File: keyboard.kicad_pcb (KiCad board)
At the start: 2 copper layers, 121 parts, among them P2 CONN_02X03, SW1 SW_PUSH, SW10 SW_PUSH, SW11 SW_PUSH, SW12 SW_PUSH, SW13 SW_PUSH, SW14 SW_PUSH, SW15 SW_PUSH, SW16 SW_PUSH, SW17 SW_PUSH, SW18 SW_PUSH, SW19 SW_PUSH, SW2 SW_PUSH, SW20 SW_PUSH, SW21 SW_PUSH, SW22 SW_PUSH, SW23 SW_PUSH, SW24 SW_PUSH, SW25 SW_PUSH, SW26 SW_PUSH, SW27 SW_PUSH, SW28 SW_PUSH, SW29 SW_PUSH, SW3 SW_PUSH, SW30 SW_PUSH, SW31 SW_PUSH, SW32 SW_PUSH, SW33 SW_PUSH, SW34 SW_PUSH, SW35 SW_PUSH, SW36 SW_PUSH, SW37 SW_PUSH, SW38 SW_PUSH, SW39 SW_PUSH, SW4 SW_PUSH, SW40 SW_PUSH, SW41 SW_PUSH, SW42 SW_PUSH, SW43 SW_PUSH, SW44 SW_PUSH, SW45 SW_PUSH, SW5 SW_PUSH, SW6 SW_PUSH, SW7 SW_PUSH, SW8 SW_PUSH, SW9 SW_PUSH, U1 ATmega32U4, X1 CRYSTAL_SMD

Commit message: right hand side initial layout
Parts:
- moved SW2 459.2 mm to (279.2, 71.5)
- moved SW4 457.2 mm to (301.9, 78.5)
- moved SW3 422.5 mm to (281.9, 84.5)
- moved SW10 411.4 mm to (237.0, 80.1)
- moved SW5 402.4 mm to (258.3, 43.3)
- moved SW9 398.5 mm to (236.2, 57.5)
- moved SW6 383.2 mm to (258.2, 62.6)
- moved SW13 379.9 mm to (217.4, 91.0)
- moved SW8 369.9 mm to (235.3, 41.0)
- moved SW15 363.8 mm to (195.7, 68.0)
- moved SW11 362.7 mm to (213.9, 50.3)
- moved SW12 362.4 mm to (214.5, 66.3)
- moved SW7 359.2 mm to (257.6, 83.1)
- moved SW14 357.2 mm to (194.3, 52.5)
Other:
- board text added: "right side"

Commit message: picoflex connectors & good idea of board layout
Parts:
- added P10: CONN_01X01, Mounting_Holes:MountingHole_3mm, F.Cu at (272.0, 115.3)
- added P3: CONN_01X01, Mounting_Holes:MountingHole_3mm, F.Cu at (92.9, 52.0)
- added P4: CONN_01X01, Mounting_Holes:MountingHole_3mm, F.Cu at (23.4, 111.4)
- added P5: CONN_01X01, Mounting_Holes:MountingHole_3mm, F.Cu at (252.5, 62.0)
- added P6: CONN_01X01, Mounting_Holes:MountingHole_3mm, F.Cu at (163.6, 100.6)
- added P7: CONN_01X01, Mounting_Holes:MountingHole_3mm, F.Cu at (201.9, 56.6)
- added P8: CONN_01X01, Mounting_Holes:MountingHole_3mm, F.Cu at (112.2, 100.8)
- added P9: CONN_01X01, Mounting_Holes:MountingHole_3mm, F.Cu at (42.4, 58.0)
- conn1, conn2: footprint Pin_Headers:Pin_Header_Straight_2x08 -> fp:PICOFLEX-90814-16
- moved D5 418.6 mm to (243.2, 75.3)
- moved D6 398.6 mm to (234.9, 94.4)
- moved D3 380.5 mm to (257.6, 100.1)
- moved D8 378.8 mm to (220.8, 70.8)
- moved D7 375.7 mm to (212.3, 70.7)
- moved led1 375.0 mm to (267.5, 101.1), turned to 86.2 degrees
- moved D2 361.8 mm to (248.2, 114.0), turned to 90 degrees
- moved D9 360.5 mm to (215.3, 89.9)
- moved D13 349.1 mm to (178.6, 82.5), turned to 180 degrees
- moved led4 347.1 mm to (227.8, 72.1), turned to 180 degrees
- moved D10 346.9 mm to (199.7, 80.8)
- moved D4 343.9 mm to (233.6, 75.2)
- moved X1 338.9 mm to (265.2, 76.5), turned to 90 degrees
- moved D14 338.3 mm to (171.2, 82.9)
- moved led2 336.5 mm to (249.2, 94.5), turned to 180 degrees
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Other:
- board text added: "left side"

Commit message: libs and thumboard components done
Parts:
- removed SW16, SW17, SW18, SW19, SW20, SW21, SW22, SW23, SW38, SW39, SW40, SW41, SW42, SW43, SW44, SW45: SW_PUSH, fp:CHERRY_MX
- added S1: alps_4way, fp:alps 4way, F.Cu at (163.1, 181.1)
- added S2: alps_4way, fp:alps 4way, F.Cu at (162.6, 165.9)
- added S3: alps_4way, fp:alps 4way, F.Cu at (130.8, 145.0)
- added S4: alps_4way, fp:alps 4way, F.Cu at (130.8, 129.3)
- added U2: psp1000, fp:-JOYSTICK-PSP1000, F.Cu at (162.8, 165.9)
- added U3: psp1000, fp:-JOYSTICK-PSP1000, F.Cu at (130.6, 129.0)
- SW1: footprint fp:CHERRY_MX -> matt:SW_SPST_FSMSM
- moved SW1 400.7 mm to (278.6, 116.8), turned to 90 degrees
- moved led10 94.8 mm to (27.4, 96.8), turned to 273.8 degrees
- moved led13 76.4 mm to (108.2, 97.3), turned to 180 degrees
- moved D43 66.2 mm to (139.4, 139.2), turned to 90 degrees
- moved led15 65.8 mm to (108.7, 77.2), turned to 45 degrees
- moved led11 59.2 mm to (88.1, 95.0), turned to 180 degrees
- moved D41 58.9 mm to (120.1, 138.4), turned to 90 degrees
- moved led12 57.7 mm to (46.2, 90.9), turned to 180 degrees
- moved D44 55.7 mm to (139.4, 149.4), turned to 90 degrees
- moved D37 55.5 mm to (122.7, 144.0), turned to 270 degrees
- moved D40 55.2 mm to (139.4, 144.3), turned to 270 degrees
- moved led14 54.3 mm to (66.8, 90.2), turned to 180 degrees
- moved D42 51.7 mm to (120.1, 143.8), turned to 90 degrees
- moved D38 45.6 mm to (119.9, 149.6), turned to 270 degrees
- moved thumb-l2 45.1 mm to (125.7, 135.4)
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
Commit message: smt 4 ways
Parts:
- S1, S2, S3, S4: footprint fp:alps 4way -> fp:alps 4way smt
- moved SW26 198.5 mm to (207.6, 42.6), turned to 183.8 degrees
- moved P4 195.9 mm to (201.2, 29.2), turned to 180 degrees
- moved D25 183.9 mm to (202.4, 51.9), turned to 180 degrees
- moved led10 177.8 mm to (197.2, 43.9), turned to 93.8 degrees
- moved SW25 167.2 mm to (188.0, 34.9), turned to 183.8 degrees
- moved D23 164.8 mm to (190.4, 43.9), turned to 180 degrees
- moved SW24 157.4 mm to (189.3, 53.8), turned to 183.8 degrees
- moved D24 147.3 mm to (181.2, 44.4), turned to 180 degrees
- moved P9 142.1 mm to (182.3, 82.7), turned to 180 degrees
- moved led12 138.5 mm to (178.4, 49.7), turned to 0 degrees
- moved SW29 124.9 mm to (167.5, 41.0), turned to 181.3 degrees
- moved D28 124.5 mm to (171.3, 50.3), turned to 180 degrees
- moved D26 122.1 mm to (173.4, 69.7), turned to 180 degrees
- moved SW27 113.4 mm to (168.3, 79.1), turned to 181.3 degrees
- moved SW28 113.1 mm to (167.9, 60.0), turned to 181.3 degrees
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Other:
- board text added: "10mm bolt with 6mm spacer"
- board text added: "even holes are 22.63 mm away from bottom edge"
- board text added: "set back 1.205mm from edge of board insulator is 2mm above top of board"

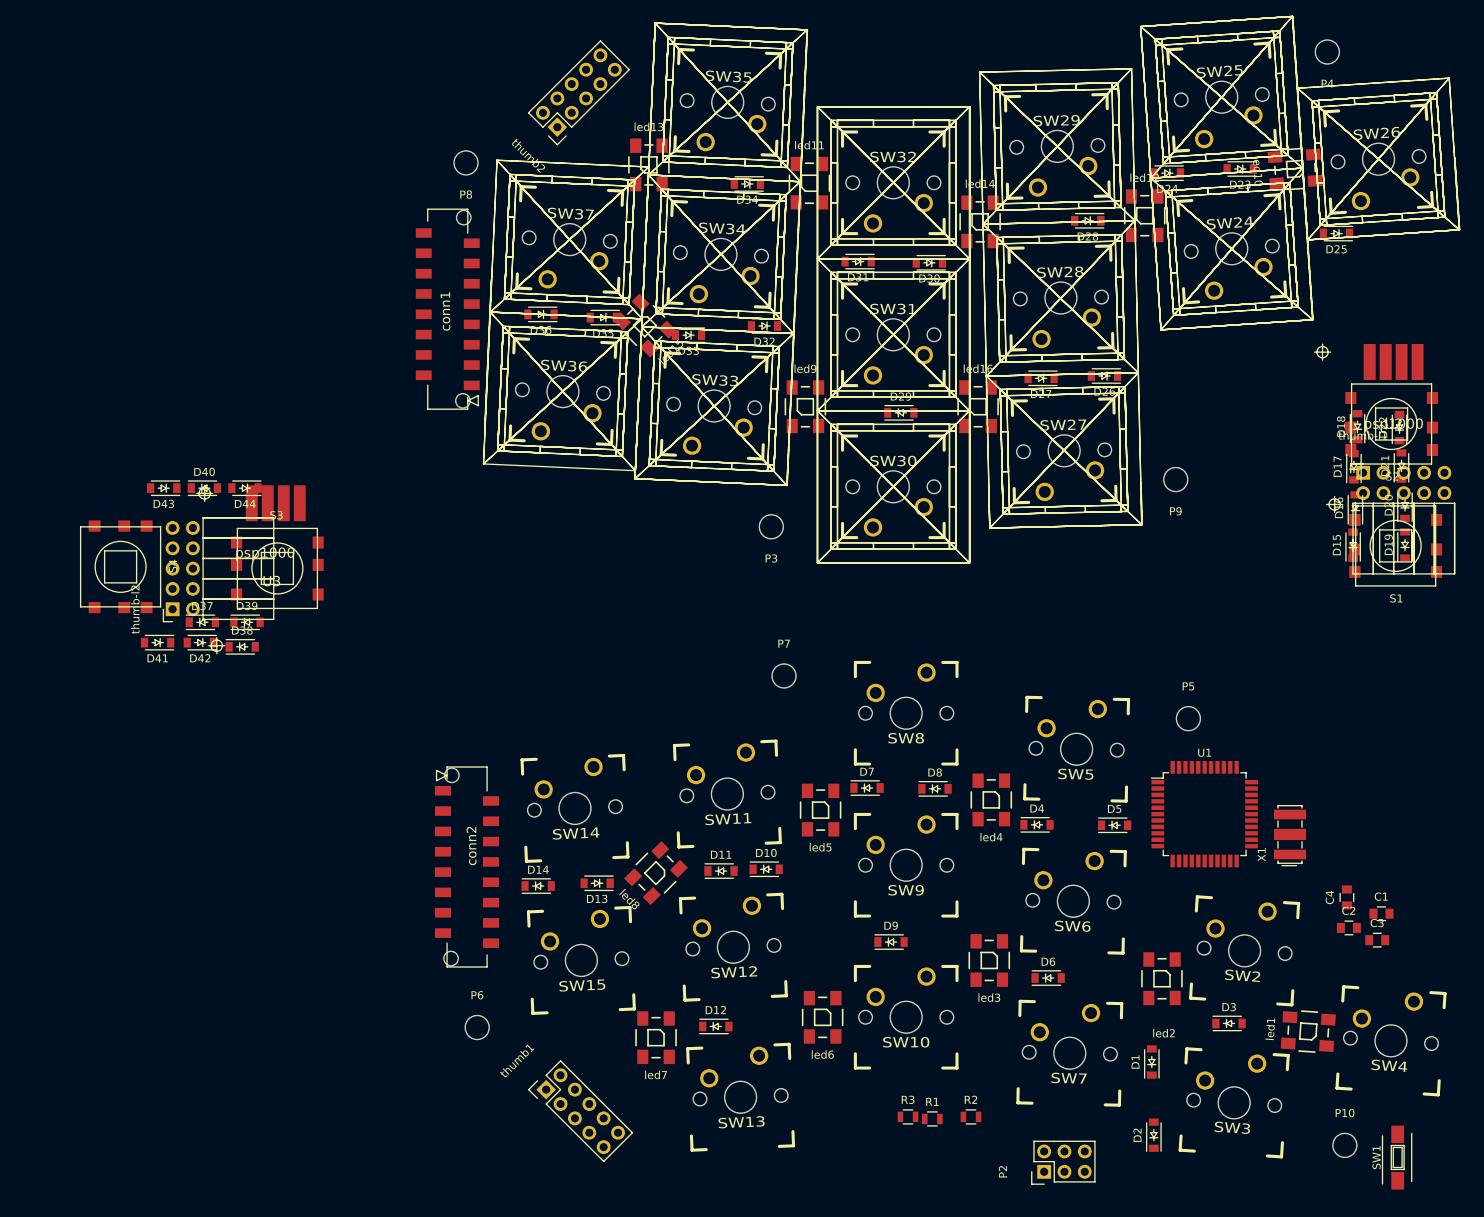
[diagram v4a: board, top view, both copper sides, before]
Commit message: removed joysticks, changed board conns, changed thumb conns
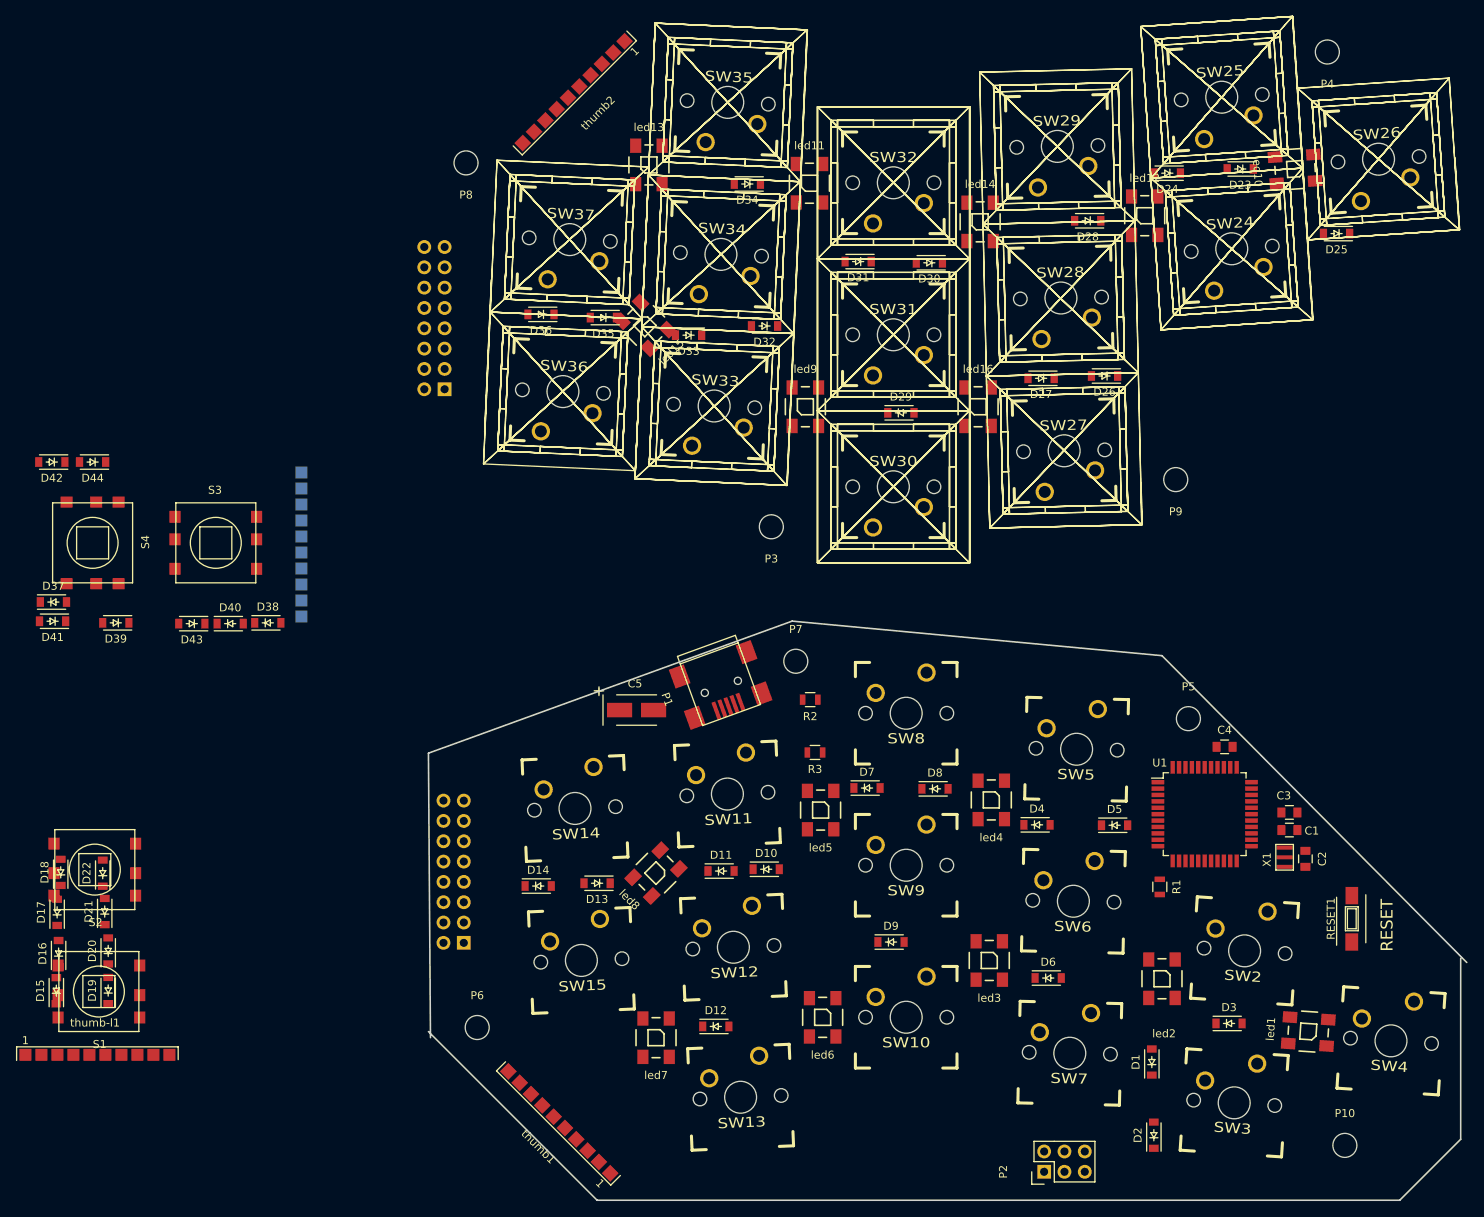
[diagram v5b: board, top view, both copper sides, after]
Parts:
- removed SW1: SW_PUSH, matt:SW_SPST_FSMSM
- removed U2, U3: psp1000, fp:-JOYSTICK-PSP1000
- added C5: 10u, Capacitors_Tantalum_SMD:TantalC_SizeB_EIA-3528_HandSoldering, F.Cu at (114.9, 111.5)
- added P1: USB_B, Connect:USB_Mini-B, F.Cu at (125.2, 107.8)
- added RESET1: SW_PUSH, matt:SW_SPST_FSMSM, F.Cu at (204.3, 137.6)
- C1: value C -> 1u
- C2: value C -> 0.1u
- X1: footprint Crystals:Resonator_7.2x3mm -> fp:cstce-v
- conn1, conn2: footprint fp:PICOFLEX-90814-16 -> Socket_Strips:Socket_Strip_Angled_2x08; moved to B.Cu
- thumb-l1: footprint Socket_Strips:Socket_Strip_Angled_2x05 -> fp:thumbpad connector
- thumb-l2: footprint Socket_Strips:Socket_Strip_Angled_2x05 -> fp:thumbpad connector; moved to B.Cu
- thumb1, thumb2: footprint Pin_Headers:Pin_Header_Straight_2x05 -> fp:thumbpad connector
- moved thumb-l1 182.4 mm to (38.5, 154.6)
- moved D15 171.4 mm to (42.4, 146.6)
- moved D17 171.4 mm to (42.5, 136.8)
- moved D18 171.4 mm to (42.9, 131.8)
- moved S2 171.4 mm to (47.2, 131.4)
- moved D16 171.4 mm to (42.7, 141.9)
- moved D19 171.4 mm to (48.9, 146.6)
- moved D20 171.4 mm to (48.9, 141.6)
- moved D21 171.4 mm to (48.4, 136.7)
- moved D22 171.4 mm to (48.2, 131.9)
- moved S1 171.4 mm to (47.7, 146.7)
- moved R2 55.9 mm to (136.6, 110.2), turned to 180 degrees
- moved R3 47.0 mm to (137.2, 116.8), turned to 180 degrees
- moved R1 40.6 mm to (180.3, 133.6), turned to 270 degrees
- moved D42 29.2 mm to (41.8, 80.5)
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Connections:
- R2 pad 2: (no net) -> Net-(P1-Pad3)
- R3 pad 2: (no net) -> Net-(P1-Pad2)
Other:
- board outline added: 129.8 x 72.4 mm
- board text added: "RESET"

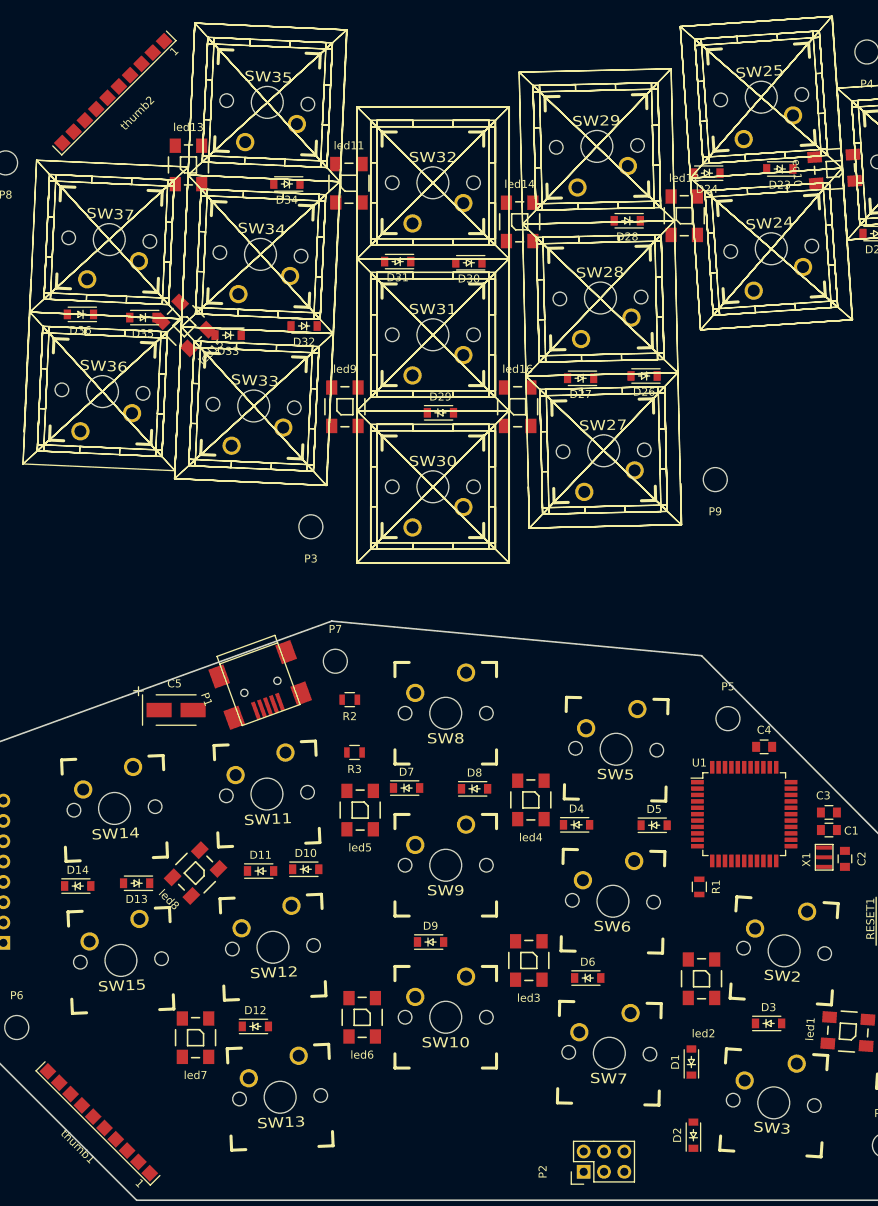
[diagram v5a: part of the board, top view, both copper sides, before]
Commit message: buttons shifted
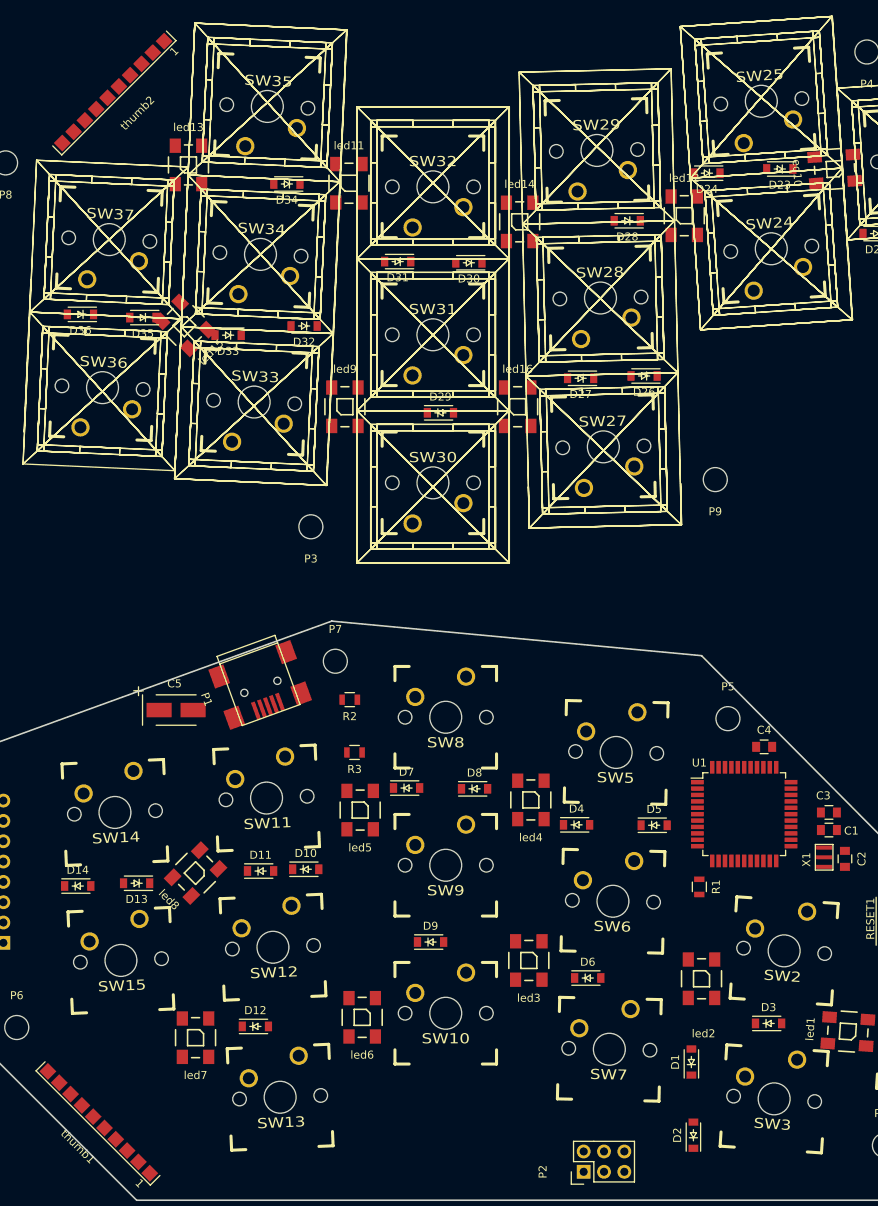
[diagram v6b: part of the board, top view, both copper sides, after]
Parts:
- moved SW25 0.51 mm to (188.1, 35.4)
- moved SW29 0.51 mm to (167.5, 41.5)
- moved SW32 0.51 mm to (147.0, 46.1)
- moved SW35 0.51 mm to (126.3, 36.0)
- moved SW3 0.50 mm to (189.7, 160.1)
- moved SW11 0.50 mm to (126.2, 122.5)
- moved SW14 0.50 mm to (107.2, 124.3)
- moved SW10 0.50 mm to (148.6, 149.4)
- moved SW7 0.50 mm to (169.1, 153.9)
- moved SW8 0.50 mm to (148.6, 112.4)
- moved SW33 0.50 mm to (124.7, 73.0)
- moved SW27 0.49 mm to (168.3, 78.6)
- moved SW30 0.49 mm to (147.0, 83.1)
- moved SW36 0.49 mm to (105.7, 71.2)
- moved SW5 0.40 mm to (169.9, 116.8)
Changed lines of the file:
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@@
     (pad_to_mask_clearance 0)
     (aux_axis_origin 0 0)
-    (visible_elements FFFFF77F)
+    (visible_elements FFFC041F)
     (pcbplotparams
       (layerselection 0x01000_00000000)
@@
   )
   (module fp:CHERRY_MX (layer F.Cu)
-    (at 189.6 160.6 356.2)
+    (at 189.65 160.1 356.2)
     (fp_text reference SW3 (at 0 3.175 356.2) (layer F.SilkS)
       (effects (font (size 1.27 1.524) (thickness 0.2032)))
@@
   )
   (module fp:CHERRY_MX (layer F.Cu)
-    (at 169.9 116.4 358.7)
+    (at 169.9 116.8 358.7)
     (fp_text reference SW5 (at 0 3.175 358.7) (layer F.SilkS)
       (effects (font (size 1.27 1.524) (thickness 0.2032)))
@@
   )
   (module fp:CHERRY_MX (layer F.Cu)
-    (at 169.05 154.4 358.7)
+    (at 169.05 153.9 358.7)
     (fp_text reference SW7 (at 0 3.175 358.7) (layer F.SilkS)
       (effects (font (size 1.27 1.524) (thickness 0.2032)))
@@
   )
   (module fp:CHERRY_MX (layer F.Cu)
-    (at 148.6 111.9)
+    (at 148.6 112.4)
     (fp_text reference SW8 (at 0 3.175) (layer F.SilkS)
       (effects (font (size 1.27 1.524) (thickness 0.2032)))
@@
   )
   (module fp:CHERRY_MX (layer F.Cu)
-    (at 148.6 149.9)
+    (at 148.6 149.4)
     (fp_text reference SW10 (at 0 3.175) (layer F.SilkS)
       (effects (font (size 1.27 1.524) (thickness 0.2032)))
@@
   )
   (module fp:CHERRY_MX (layer F.Cu)
-    (at 126.25 122 2.5)
+    (at 126.2 122.5 2.5)
     (fp_text reference SW11 (at 0 3.175 2.5) (layer F.SilkS)
       (effects (font (size 1.27 1.524) (thickness 0.2032)))
@@
   )
   (module fp:CHERRY_MX (layer F.Cu)
-    (at 107.2 123.8 2.5)
+    (at 107.25 124.3 2.5)
     (fp_text reference SW14 (at 0 3.175 2.5) (layer F.SilkS)
       (effects (font (size 1.27 1.524) (thickness 0.2032)))
@@
   )
   (module fp:CHERRY_MX (layer F.Cu)
-    (at 188.043 34.893 183.8)
+    (at 188.05 35.4 183.8)
     (fp_text reference SW25 (at 0 3.175 183.8) (layer F.SilkS)
       (effects (font (size 1.27 1.524) (thickness 0.2032)))
@@
   )
   (module fp:CHERRY_MX (layer F.Cu)
-    (at 168.343 79.093 181.3)
+    (at 168.3 78.6 181.3)
     (fp_text reference SW27 (at 0 3.175 181.3) (layer F.SilkS)
       (effects (font (size 1.27 1.524) (thickness 0.2032)))
@@
   )
   (module fp:CHERRY_MX (layer F.Cu)
-    (at 167.493 41.043 181.3)
+    (at 167.5 41.55 181.3)
     (fp_text reference SW29 (at 0 3.175 181.3) (layer F.SilkS)
       (effects (font (size 1.27 1.524) (thickness 0.2032)))
@@
   )
   (module fp:CHERRY_MX (layer F.Cu)
-    (at 146.993 83.593 180)
+    (at 147 83.1 180)
     (fp_text reference SW30 (at 0 3.175 180) (layer F.SilkS)
       (effects (font (size 1.27 1.524) (thickness 0.2032)))
@@
   )
   (module fp:CHERRY_MX (layer F.Cu)
-    (at 146.993 45.593 180)
+    (at 147 46.1 180)
     (fp_text reference SW32 (at 0 3.175 180) (layer F.SilkS)
       (effects (font (size 1.27 1.524) (thickness 0.2032)))
@@
   )
   (module fp:CHERRY_MX (layer F.Cu)
-    (at 124.593 73.493 177.5)
+    (at 124.65 73 177.5)
     (fp_text reference SW33 (at 0 3.175 177.5) (layer F.SilkS)
       (effects (font (size 1.27 1.524) (thickness 0.2032)))
@@
   )
   (module fp:CHERRY_MX (layer F.Cu)
-    (at 126.293 35.543 177.5)
+    (at 126.3 36.05 177.5)
     (fp_text reference SW35 (at 0 3.175 177.5) (layer F.SilkS)
       (effects (font (size 1.27 1.524) (thickness 0.2032)))
@@
   )
   (module fp:CHERRY_MX (layer F.Cu)
-    (at 105.693 71.693 177.5)
+    (at 105.7 71.2 177.5)
     (fp_text reference SW36 (at 0 3.175 177.5) (layer F.SilkS)
       (effects (font (size 1.27 1.524) (thickness 0.2032)))
